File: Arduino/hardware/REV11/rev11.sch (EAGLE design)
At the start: 28 parts, among them IC2 ATMEGA168-AU, Q1 32768Hz

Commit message: bringing things back in sync
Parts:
- renumbered R1 to R1********
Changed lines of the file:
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@@
 <part name="P+5" library="SparkFun-Aesthetics" deviceset="VCC" device=""/>
 <part name="GND7" library="SparkFun-Aesthetics" deviceset="GND" device=""/>
-<part name="R1" library="resistor" deviceset="R-EU_" device="R0603" value="220K"/>
+<part name="R1********" library="resistor" deviceset="R-EU_" device="R0603" value="220K"/>
 <part name="R9" library="resistor" deviceset="R-EU_" device="R0603" value="4.7K"/>
 <part name="P+1" library="SparkFun-Aesthetics" deviceset="VCC" device=""/>
@@
 <instance part="P+5" gate="G$1" x="25.4" y="243.84"/>
 <instance part="GND7" gate="1" x="180.34" y="187.96"/>
-<instance part="R1" gate="G$1" x="187.96" y="190.5" rot="R180"/>
+<instance part="R1********" gate="G$1" x="187.96" y="190.5" rot="R180"/>
 <instance part="R9" gate="G$1" x="236.22" y="175.26" smashed="yes">
 <attribute name="NAME" x="237.49" y="176.7586" size="1.778" layer="95"/>
@@
 <pinref part="GND7" gate="1" pin="GND"/>
 <wire x1="180.34" y1="190.5" x2="182.88" y2="190.5" width="0.1524" layer="91"/>
-<pinref part="R1" gate="G$1" pin="2"/>
+<pinref part="R1********" gate="G$1" pin="2"/>
 </segment>
 <segment>
@@
 <net name="LDR" class="0">
 <segment>
-<pinref part="R1" gate="G$1" pin="1"/>
+<pinref part="R1********" gate="G$1" pin="1"/>
 <wire x1="198.12" y1="190.5" x2="198.12" y2="186.944" width="0.1524" layer="91"/>
 <wire x1="193.04" y1="190.5" x2="198.12" y2="190.5" width="0.1524" layer="91"/>

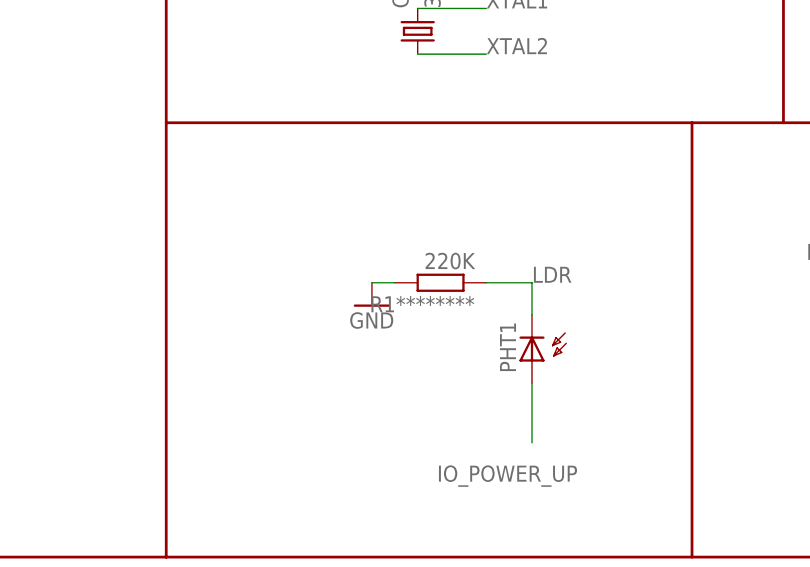
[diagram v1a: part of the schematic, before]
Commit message: rev10 and rev11 routed again
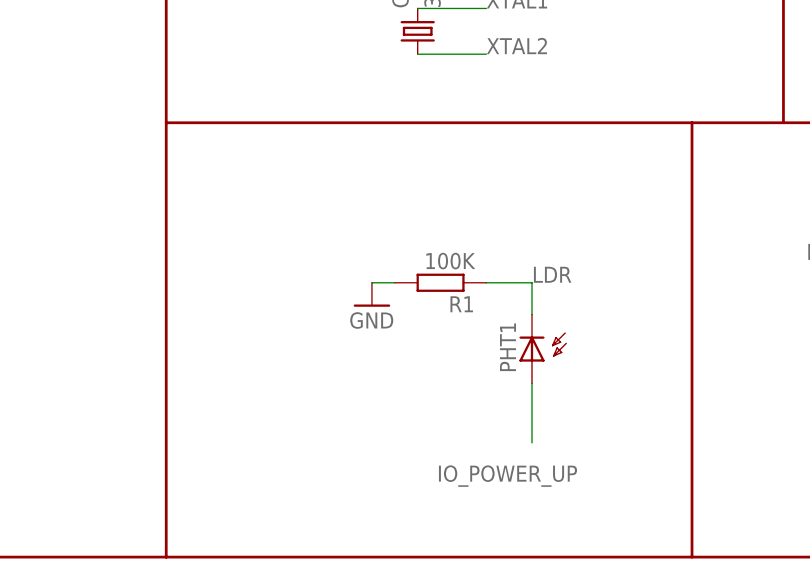
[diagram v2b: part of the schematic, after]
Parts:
- R1: value 220K -> 100K
- renumbered R1******** to R1
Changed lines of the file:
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@@
 <part name="P+5" library="SparkFun-Aesthetics" deviceset="VCC" device=""/>
 <part name="GND7" library="SparkFun-Aesthetics" deviceset="GND" device=""/>
-<part name="R1********" library="resistor" deviceset="R-EU_" device="R0603" value="220K"/>
+<part name="R1" library="resistor" deviceset="R-EU_" device="R0603" value="100K"/>
 <part name="R9" library="resistor" deviceset="R-EU_" device="R0603" value="4.7K"/>
 <part name="P+1" library="SparkFun-Aesthetics" deviceset="VCC" device=""/>
@@
 <instance part="P+5" gate="G$1" x="25.4" y="243.84"/>
 <instance part="GND7" gate="1" x="180.34" y="187.96"/>
-<instance part="R1********" gate="G$1" x="187.96" y="190.5" rot="R180"/>
+<instance part="R1" gate="G$1" x="187.96" y="190.5" rot="R180"/>
 <instance part="R9" gate="G$1" x="236.22" y="175.26" smashed="yes">
 <attribute name="NAME" x="237.49" y="176.7586" size="1.778" layer="95"/>
@@
 <pinref part="GND7" gate="1" pin="GND"/>
 <wire x1="180.34" y1="190.5" x2="182.88" y2="190.5" width="0.1524" layer="91"/>
-<pinref part="R1********" gate="G$1" pin="2"/>
+<pinref part="R1" gate="G$1" pin="2"/>
 </segment>
 <segment>
@@
 <net name="LDR" class="0">
 <segment>
-<pinref part="R1********" gate="G$1" pin="1"/>
+<pinref part="R1" gate="G$1" pin="1"/>
 <wire x1="198.12" y1="190.5" x2="198.12" y2="186.944" width="0.1524" layer="91"/>
 <wire x1="193.04" y1="190.5" x2="198.12" y2="190.5" width="0.1524" layer="91"/>

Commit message: rev10 and 11 updated as per deniz findings
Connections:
- net D2: now also I2C_EXT.14
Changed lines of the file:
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@@
 <layer number="97" name="Info" color="7" fill="1" visible="yes" active="yes"/>
 <layer number="98" name="Guide" color="6" fill="1" visible="yes" active="yes"/>
+<layer number="99" name="SpiceOrder" color="5" fill="1" visible="yes" active="yes"/>
 <layer number="100" name="Muster" color="7" fill="1" visible="no" active="no"/>
 <layer number="101" name="Patch_Top" color="12" fill="4" visible="no" active="yes"/>
@@
 <wire x1="127" y1="231.14" x2="127" y2="218.44" width="0.1524" layer="91"/>
 <label x="129.54" y="231.14" size="1.778" layer="95"/>
-</segment>
-</net>
+<pinref part="I2C_EXT" gate="A" pin="14"/>
+</segment>
+</net>
